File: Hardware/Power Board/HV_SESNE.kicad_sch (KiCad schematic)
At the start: 69 parts, among them IC7 ISO6762FDWR, IC8 ADS131M08QPBSRQ1, U4 L78L33_SOT89

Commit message: Ditched ASC
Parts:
- C24: value C_Small -> 1uF-25V-10%-0603
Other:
- moved on the sheet: C24
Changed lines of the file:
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@@
   (junction (at 180.975 129.54) (diameter 0) (color 0 0 0 0)
   )
-  (junction (at 107.315 186.69) (diameter 0) (color 0 0 0 0)
-  )
   (junction (at 120.65 186.69) (diameter 0) (color 0 0 0 0)
   )
@@
   (junction (at 24.765 68.58) (diameter 0) (color 0 0 0 0)
   )
+  (junction (at 99.06 186.69) (diameter 0) (color 0 0 0 0)
+  )
   (junction (at 34.29 68.58) (diameter 0) (color 0 0 0 0)
   )
@@
   (junction (at 34.925 119.38) (diameter 0) (color 0 0 0 0)
   )
+  (junction (at 99.06 175.26) (diameter 0) (color 0 0 0 0)
+  )
   (junction (at 152.4 175.26) (diameter 0) (color 0 0 0 0)
   )
@@
   (junction (at 33.655 93.98) (diameter 0) (color 0 0 0 0)
   )
-  (junction (at 107.315 175.26) (diameter 0) (color 0 0 0 0)
-  )
   (junction (at 34.29 55.88) (diameter 0) (color 0 0 0 0)
   )
@@
   (junction (at 186.055 27.305) (diameter 0) (color 0 0 0 0)
   )
-  (wire (pts (xy 107.315 186.69) (xy 120.65 186.69))
+  (wire (pts (xy 99.06 186.69) (xy 120.65 186.69))
     (stroke (width 0) (type default))
   )
@@
     (stroke (width 0) (type default))
   )
-  (wire (pts (xy 107.315 175.26) (xy 103.505 175.26))
+  (wire (pts (xy 99.06 175.26) (xy 95.25 175.26))
     (stroke (width 0) (type default))
   )
@@
     (stroke (width 0) (type default))
   )
-  (wire (pts (xy 107.315 175.26) (xy 113.03 175.26))
+  (wire (pts (xy 99.06 175.26) (xy 113.03 175.26))
     (stroke (width 0) (type default))
   )
@@
     (stroke (width 0) (type default))
   )
-  (wire (pts (xy 107.315 186.69) (xy 107.315 183.515))
+  (wire (pts (xy 99.06 186.69) (xy 99.06 183.515))
     (stroke (width 0) (type default))
   )
@@
     (stroke (width 0) (type default))
   )
-  (wire (pts (xy 103.505 186.69) (xy 107.315 186.69))
+  (wire (pts (xy 95.25 186.69) (xy 99.06 186.69))
     (stroke (width 0) (type default))
   )
@@
     (stroke (width 0) (type default))
   )
-  (wire (pts (xy 107.315 178.435) (xy 107.315 175.26))
+  (wire (pts (xy 99.06 178.435) (xy 99.06 175.26))
     (stroke (width 0) (type default))
   )
@@
     (effects (font (size 1.27 1.27)) (justify right))
   )
-  (hierarchical_label "ISO_0V" (shape input) (at 103.505 186.69 180) (fields_autoplaced)
+  (hierarchical_label "ISO_0V" (shape input) (at 95.25 186.69 180) (fields_autoplaced)
     (effects (font (size 1.27 1.27)) (justify right))
   )
@@
     (effects (font (size 1.27 1.27)) (justify right))
   )
-  (hierarchical_label "ISO_15V" (shape output) (at 103.505 175.26 180) (fields_autoplaced)
+  (hierarchical_label "ISO_15V" (shape output) (at 95.25 175.26 180) (fields_autoplaced)
     (effects (font (size 1.27 1.27)) (justify right))
   )
@@
     )
   )
-  (symbol (lib_id "Device:C_Small") (at 107.315 180.975 0) (unit 1)
-    (in_bom yes) (on_board yes) (dnp no) (fields_autoplaced)
-    (property "Reference" "C24" (at 109.855 179.7112 0)
+  (symbol (lib_id "Device:C_Small") (at 99.06 180.975 0) (unit 1)
+    (in_bom yes) (on_board yes) (dnp no) (fields_autoplaced)
+    (property "Reference" "C24" (at 102.235 180.3463 0)
       (effects (font (size 0.75 0.75)) (justify left))
     )
-    (property "Value" "C_Small" (at 109.855 182.2512 0)
+    (property "Value" "1uF-25V-10%-0603" (at 102.235 181.6163 0)
       (effects (font (size 0.75 0.75)) (justify left))
     )
-    (property "Footprint" "" (at 107.315 180.975 0)
-      (effects (font (size 1.27 1.27)) hide)
-    )
-    (property "Datasheet" "~" (at 107.315 180.975 0)
-      (effects (font (size 1.27 1.27)) hide)
-    )
+    (property "Footprint" "" (at 99.06 180.975 0)
+      (effects (font (size 1.27 1.27)) hide)
+    )
+    (property "Datasheet" "~" (at 99.06 180.975 0)
+      (effects (font (size 1.27 1.27)) hide)
+    )

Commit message: Board Layout Almost Done, about to remove Kelvin source due to concerns about uneven current sharing
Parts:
- C15, C16, C17, C18, C19, C20, C21, C22: value C_Small -> DNP; footprint (none) -> Capacitor_SMD:C_0603_1608Metric
- C23, C26, C27, C28: value 100nF-25V-10%-0603 -> 100nF-50V-10%-0603; footprint (none) -> Capacitor_SMD:C_0603_1608Metric
- C24, C25, C29, C31: value 1uF-25V-10%-0603 -> 1uF-25V-10%-0805; footprint (none) -> Capacitor_SMD:C_0805_2012Metric
- C30: value 220nF-25V-10%-0603 -> 1uF-25V-10%-08051uF-25V-10%-0805; footprint (none) -> Capacitor_SMD:C_0805_2012Metric
- FB1: footprint (none) -> Resistor_SMD:R_0603_1608Metric
- IC8: footprint QFP50P700X700X120-32N -> SamacSys_Parts:QFP50P700X700X120-32N
- R35, R36, R37, R38, R39, R40, R41, R42, R43, R44, R45, R46, R47, R48, R49, R50, R51, R52, R53, R54, R55, R56, R57, R58, R59, R60, R61, R62, R63, R64, R65, R66, R67, R68, R69, R70, R71, R72, R73, R74, R75, R76, R77, R78, R79, R80, R81, R82: footprint (none) -> Resistor_SMD:R_1206_3216Metric

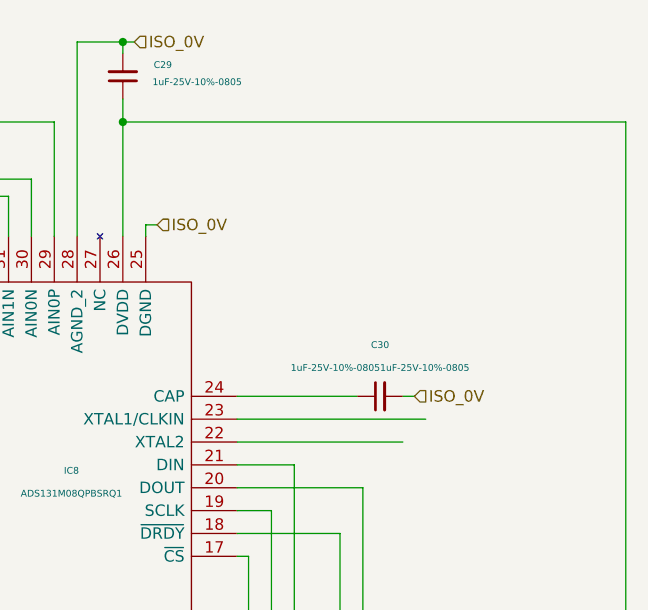
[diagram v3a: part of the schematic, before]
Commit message: Finished intial LV board connector routing, going to tear up current sense and redo
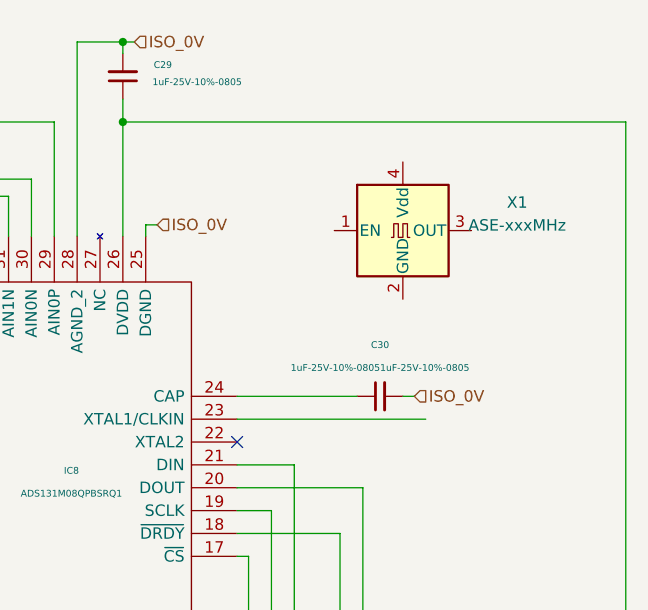
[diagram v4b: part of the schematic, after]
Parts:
- added X1: ASE-xxxMHz, Oscillator:Oscillator_SMD_Abracon_ASE-4Pin_3.2x2.5mm, symbol Oscillator:ASE-xxxMHz
- IC8: footprint SamacSys_Parts:QFP50P700X700X120-32N -> QFP50P700X700X120-32N
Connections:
- no-connect marks 0 -> 1
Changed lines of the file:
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@@
   (junction (at 186.055 27.305) (diameter 0) (color 0 0 0 0)
   )
+  (no_connect (at 198.755 71.755))
   (wire (pts (xy 99.06 186.69) (xy 120.65 186.69))
     (stroke (width 0) (type default))
@@
   )
   (wire (pts (xy 22.86 30.48) (xy 24.765 30.48))
-    (stroke (width 0) (type default))
-  )
-  (wire (pts (xy 217.17 71.755) (xy 198.755 71.755))
     (stroke (width 0) (type default))
   )
@@
     )
   )
+  (symbol (lib_id "Oscillator:ASE-xxxMHz") (at 217.17 48.26 0) (unit 1)
+    (in_bom yes) (on_board yes) (dnp no) (fields_autoplaced)
+    (property "Reference" "X1" (at 229.87 45.1359 0)
+      (effects (font (size 1.27 1.27)))
+    )
+    (property "Value" "ASE-xxxMHz" (at 229.87 47.6759 0)
+      (effects (font (size 1.27 1.27)))
+    )
+    (property "Footprint" "Oscillator:Oscillator_SMD_Abracon_ASE-4Pin_3.2x2.5mm" (at 234.95 57.15 0)
+      (effects (font (size 1.27 1.27)) hide)
+    )
+    (property "Datasheet" "http://www.abracon.com/Oscillators/ASV.pdf" (at 214.63 48.26 0)
+      (effects (font (size 1.27 1.27)) hide)
+    )
+    (pin "1")
+    (pin "2")
+    (pin "3")
+    (pin "4")
+    (instances
+      (project "Power Board"
+        (path "/6be5afcf-5319-4edd-874e-36cb4fffe262/791fb412-fe5d-424f-bd04-f24cb7e8276c"
+          (reference "X1") (unit 1)
+        )
+      )
+    )
+  )
   (symbol (lib_id "Device:C_Small") (at 99.06 180.975 0) (unit 1)
     (in_bom yes) (on_board yes) (dnp no) (fields_autoplaced)
@@
       (effects (font (size 0.75 0.75)))
     )
-    (property "Footprint" "SamacSys_Parts:QFP50P700X700X120-32N" (at 194.945 53.975 0)
+    (property "Footprint" "QFP50P700X700X120-32N" (at 194.945 53.975 0)
       (effects (font (size 1.27 1.27)) (justify left) hide)
     )
